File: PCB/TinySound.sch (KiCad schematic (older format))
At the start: 20 parts, among them J1 Conn_01x02, J2 Conn_01x02, J3 Micro_SD_Card_Det, J4 Conn_01x04, J5 Conn_01x02, U1 MAX98360AENL+, U2 STM32G030KxT, U3 MAX98360xxxB+

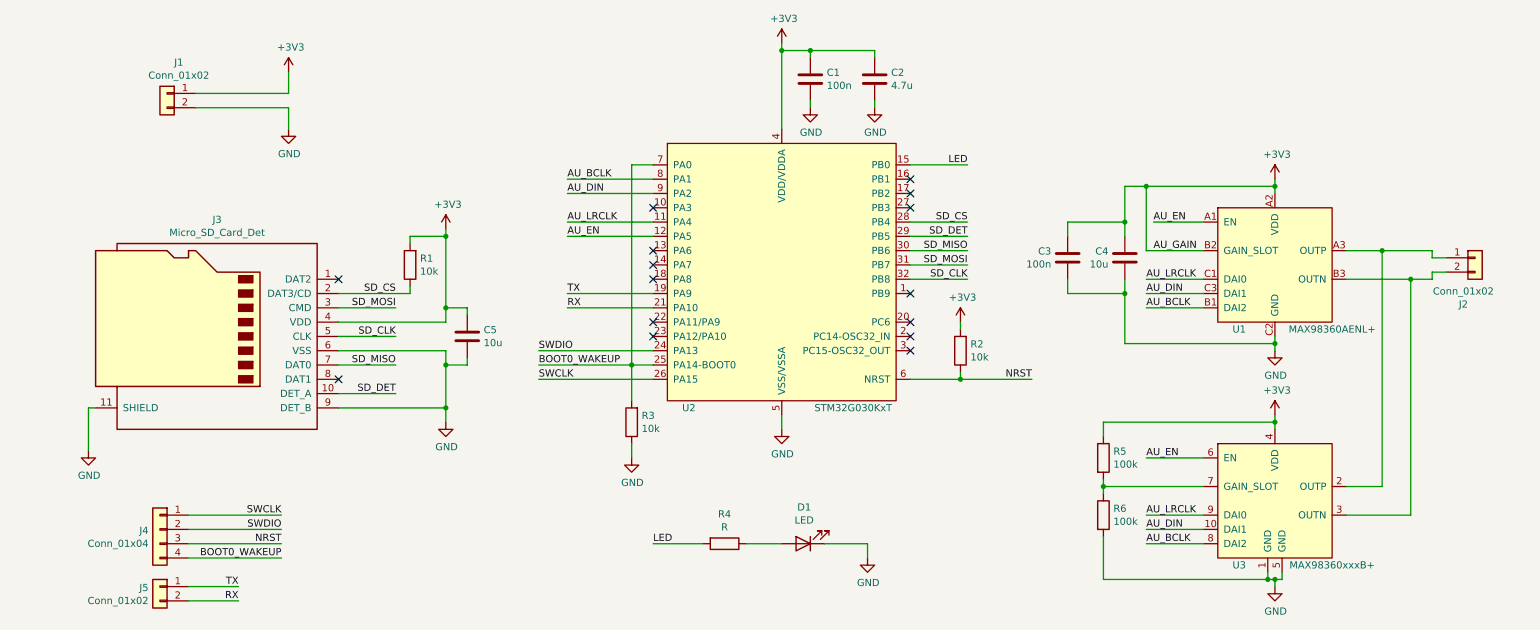
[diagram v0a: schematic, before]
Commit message: [PCB] Additional resistors for SD card
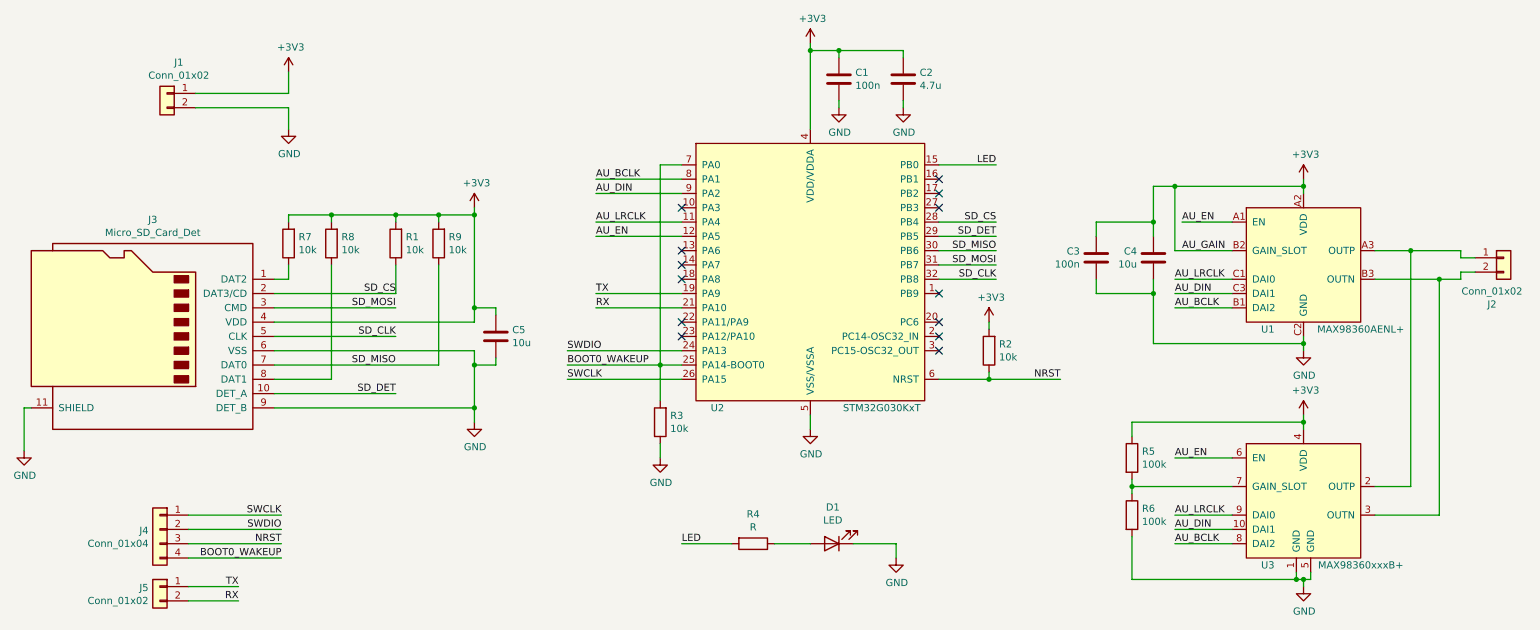
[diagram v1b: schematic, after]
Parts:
- added R7, R8, R9: 10k, Resistor_SMD:R_0603_1608Metric, symbol Device:R
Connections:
- net +3V3: now also R7.2, R8.2, R9.2
- net SD_MISO: now also R9.1
- net at J3.1 (DAT2): now also R7.1
- net at J3.8 (DAT1): now also R8.1
- no-connect marks 15 -> 13
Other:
- moved on the sheet: C1, C2, C3, C4, C5, D1, J2, J3, R1, R2, R3, R4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

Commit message: [PCB] Fixed wiring error for SWD
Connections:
- net NRST: now also J4.2 (Pin_2); no longer J4.3 (Pin_3)
- net SWDIO: now also J4.3 (Pin_3); no longer J4.2 (Pin_2)
- net BOOT0_WAKEUP renamed SWCLK_BOOT0_WAKEUP
- net SWCLK renamed GPIO
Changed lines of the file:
@@
 Text Label 7900 3500 2    50   ~ 0
 NRST
-Text Label 2450 4650 2    50   ~ 0
+Text Label 2450 4550 2    50   ~ 0
 NRST
 $Comp
@@
 	-1   0    0    -1
 $EndComp
-Text Label 2450 4550 2    50   ~ 0
+Text Label 2450 4650 2    50   ~ 0
 SWDIO
-Text Label 2450 4450 2    50   ~ 0
-SWCLK
-Wire Wire Line
-	2450 4450 1800 4450
 Wire Wire Line
 	1800 4550 2450 4550
@@
 	-1   0    0    -1
 $EndComp
-Text Label 2450 4750 2    50   ~ 0
-BOOT0_WAKEUP
-Wire Wire Line
-	2450 4750 1800 4750
-Text Label 4450 3400 0    50   ~ 0
-BOOT0_WAKEUP
-Wire Wire Line
-	4450 3400 5100 3400
+Text Label 4200 3400 0    50   ~ 0
+SWCLK_BOOT0_WAKEUP
+Wire Wire Line
+	4200 3400 5100 3400
 $Comp
 L Device:R R3
@@
 NoConn ~ 5250 3200
 Wire Wire Line
-	5250 3500 4450 3500
-Wire Wire Line
 	4450 3300 5250 3300
 Text Label 4450 3300 0    50   ~ 0
 SWDIO
-Text Label 4450 3500 0    50   ~ 0
-SWCLK
 Text Label 7450 2400 2    50   ~ 0
 SD_CS
@@
 	2500 2350 2800 2350
 Connection ~ 2800 2350
+Wire Wire Line
+	2750 4750 1800 4750
+Text Label 2750 4750 2    50   ~ 0
+SWCLK_BOOT0_WAKEUP
+Wire Wire Line
+	2450 4450 1800 4450
+Text Label 2450 4450 2    50   ~ 0
+GPIO
+Text Label 4450 3500 0    50   ~ 0
+GPIO
+Wire Wire Line
+	4450 3500 5250 3500
 $EndSCHEMATC

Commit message: [PCB] Minor tweaks
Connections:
- net NRST: now also J4.4 (Pin_4); no longer J4.2 (Pin_2)
- net SWCLK_BOOT0_WAKEUP: now also J4.3 (Pin_3); no longer J4.4 (Pin_4)
- net SWDIO: now also J4.2 (Pin_2); no longer J4.3 (Pin_3)
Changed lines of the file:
@@
 Text Label 7900 3500 2    50   ~ 0
 NRST
-Text Label 2450 4550 2    50   ~ 0
+Text Label 2450 4750 2    50   ~ 0
 NRST
 $Comp
@@
 	-1   0    0    -1
 $EndComp
-Text Label 2450 4650 2    50   ~ 0
+Text Label 2450 4550 2    50   ~ 0
 SWDIO
 Wire Wire Line
 	1800 4550 2450 4550
 Wire Wire Line
-	2450 4650 1800 4650
+	2750 4650 1800 4650
 Text Label 2150 4950 2    50   ~ 0
 TX
@@
 Connection ~ 2800 2350
 Wire Wire Line
-	2750 4750 1800 4750
-Text Label 2750 4750 2    50   ~ 0
+	2450 4750 1800 4750
+Text Label 2750 4650 2    50   ~ 0
 SWCLK_BOOT0_WAKEUP
 Wire Wire Line

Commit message: [PCB] Generated interactive HTML BOM
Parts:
- U1: footprint Package_BGA:Maxim_WLP-9_1.595x1.415_Layout3x3_P0.4mm_Ball0.27mm_Pad0.25mm_NSMD -> TinySound:Maxim_WLP-9_1.595x1.415_Layout3x3_P0.4mm_Ball0.27mm_Pad0.25mm_NSMD
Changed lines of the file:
@@
 F 0 "U1" H 9350 2250 50  0000 C CNN
 F 1 "MAX98360AENL+" H 10000 2250 50  0000 C CNN
-F 2 "Package_BGA:Maxim_WLP-9_1.595x1.415_Layout3x3_P0.4mm_Ball0.27mm_Pad0.25mm_NSMD" H 9600 1400 50  0001 C CNN
+F 2 "TinySound:Maxim_WLP-9_1.595x1.415_Layout3x3_P0.4mm_Ball0.27mm_Pad0.25mm_NSMD" H 9600 1400 50  0001 C CNN
 F 3 "https://datasheets.maximintegrated.com/en/ds/MAX98360A-MAX98360D.pdf" H 9500 2100 50  0001 C CNN
 F 4 "3288145" H 9600 1400 50  0001 C CNN "Farnell"
